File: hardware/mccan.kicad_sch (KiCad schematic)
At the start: 0 parts

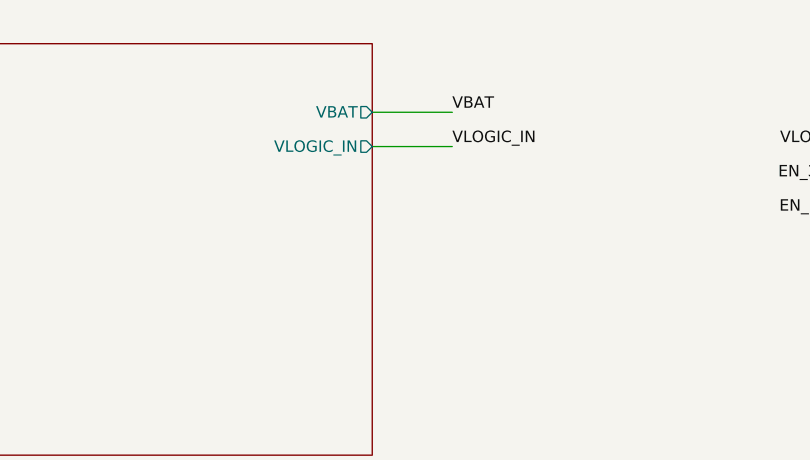
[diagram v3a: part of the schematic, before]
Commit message: hw: J1 to 3-way, IGN_IN on cavity 1 for the battery-feed topology
The Experia's peripheral outlet closes all 12 V at shut-off, so the shipped build
(topology A) needs no ignition signal at all.  This provisions the third cavity
so a battery-fed installation (topology B) is a harness change plus populating
R37/R38, rather than a new panel: Superseal 1.5 2-way and 3-way are different
cutouts, so it could not have been retrofitted.

The third cavity went ABOVE the existing two, not below.  GND_IN drops vertically
from pin 2 at x=31.75 down to y=101.6, so a pin placed below would have landed on
that wire and shorted IGN_IN to ground.  Placing it above left every existing
wire, junction and net on this verified sheet untouched.  Verified from the
netlist: FEED_P and GND_IN keep exactly their previous membership, and GND_IN is
still separate from GND, so the common-mode choke split is intact.  The pins
renumber as a consequence - 1 = IGN_IN, 2 = +12 V, 3 = GND - and cavity 1 being
an end cavity is the easy one to plug.

Adds C40, 100 nF on IGN_SENSE.  IGN_IN is an unshielded 12 V wire entering a
sealed enclosure onto a high-impedance node; C40 forms an RC with R37 giving
tau ~ 2 ms, which costs nothing against an ignition signal that changes over
seconds.  Flagged in part-selection.md as an addition.

Also records a real inconsistency found on the way: power_input has no working
generator.  The scratchpad gen.py lost its notes module to a filename collision,
and once reconstructed it emitted a materially different file from the committed
sheet, so this change was made by surgical text edit and the stale generator was
deliberately not committed.

ERC 25 -> 23 violations; the two IGN_IN single-pin warnings cleared now that the
net has a real source and a real consumer.  The remaining 23 are all the outputs
sheet, which does not exist yet.

Co-Authored-By: Claude Opus 5 <noreply@anthropic.com>
Claude-Session: https://claude.ai/code/session_01Bkq7QP4he4cdfxkUNzx7DL
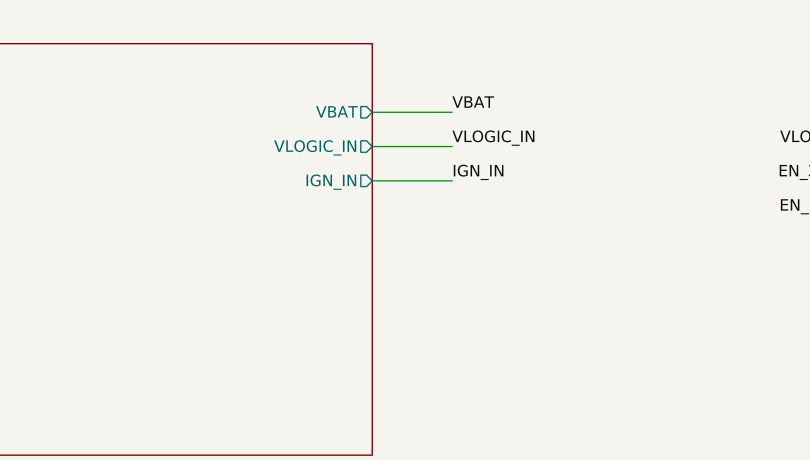
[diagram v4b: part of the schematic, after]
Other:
- sheet power_input ports: added IGN_IN; removed none
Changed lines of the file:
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@@
+	(wire
+		(pts
+			(xy 101.6 55.88) (xy 110.49 55.88)
+		)
+		(stroke
+			(width 0)
+			(type default)
+		)
+	)
 	(wire
 		(pts
@@
 	(label "VLOGIC_IN"
 		(at 110.49 52.07 0)
+		(effects
+			(font
+				(size 1.27 1.27)
+			)
+			(justify left bottom)
+		)
+	)
+	(label "IGN_IN"
+		(at 110.49 55.88 0)
 		(effects
 			(font
@@
 			(effects
 				(font
+					(size 1.27 1.27)
+				)
+				(justify left)
+			)
+		)
+		(pin "IGN_IN" output
+			(at 101.6 55.88 0)
+			(effects
+				(font
